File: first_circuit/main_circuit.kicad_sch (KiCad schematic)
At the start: 1 part

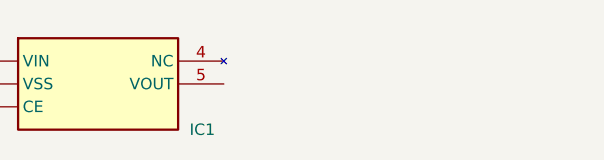
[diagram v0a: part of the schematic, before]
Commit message: need to create nets first
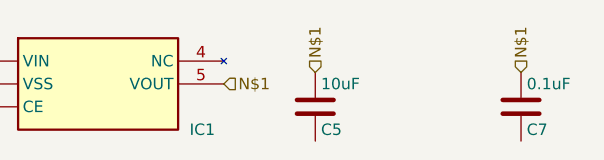
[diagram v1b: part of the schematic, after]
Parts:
- added C5: 10uF, Capacitor_SMD:C_0603, symbol Device:C
- added C7: 0.1uF, Capacitor_SMD:C_0603, symbol Device:C
- IC1: hierarchy_path /4697b12b-0876-4ea0-b477-ab5805670aa4 -> /acfeb8ae-789f-47ff-9243-69ba4f706be6; root_uuid 4697b12b-0876-4ea0-b477-ab5805670aa4 -> acfeb8ae-789f-47ff-9243-69ba4f706be6
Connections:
- net N$1: now reaches IC1.5 (VOUT)
- net N$1: now also C5.1, C7.1
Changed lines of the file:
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@@
 			)
 		)
-		(property "hierarchy_path" "/4697b12b-0876-4ea0-b477-ab5805670aa4"
+		(property "hierarchy_path" "/acfeb8ae-789f-47ff-9243-69ba4f706be6"
 			(at 43.18 33.0199 0)
 			(effects
@@
 			)
 		)
-		(property "root_uuid" "4697b12b-0876-4ea0-b477-ab5805670aa4"
+		(property "root_uuid" "acfeb8ae-789f-47ff-9243-69ba4f706be6"
 			(at 43.18 33.0199 0)
 			(effects
@@
 		(instances
 			(project ""
-				(path "/4697b12b-0876-4ea0-b477-ab5805670aa4"
+				(path "/acfeb8ae-789f-47ff-9243-69ba4f706be6"
 					(reference "IC1")
 					(unit 1)
@@
 		)
 	)
+	(symbol
+		(lib_id "Device:C")
+		(at 78.74 33.02 0)
+		(unit 1)
+		(exclude_from_sim no)
+		(in_bom yes)
+		(on_board yes)
+		(dnp no)
+		(fields_autoplaced no)
+		(property "Reference" "C5"
+			(at 79.375 35.56 0.0000)
+			(effects
+				(font
+					(size 1.27 1.27)
+				)
+				(justify left)
+			)
+		)
+		(property "Value" "10uF"
+			(at 79.375 30.48 0.0000)
+			(effects
+				(font
+					(size 1.27 1.27)
+				)
+				(justify left)
+			)
+		)
+		(property "Footprint" "Capacitor_SMD:C_0603"
+			(at 79.7052 29.21 0.0000)
+			(effects
+				(font
+					(size 1.27 1.27)
+				)
+				(hide yes)
+			)
+		)
+		(property "hierarchy_path" "/acfeb8ae-789f-47ff-9243-69ba4f706be6"
+			(at 81.28 38.0999 0)
+			(effects
+				(font
+					(size 1.27 1.27)
+				)
+				(hide yes)
+			)
+		)
+		(property "project_name" "main_circuit"
+			(at 81.28 38.0999 0)
+			(effects
+				(font
+					(size 1.27 1.27)
+				)
+				(hide yes)
+			)
+		)
+		(property "root_uuid" "acfeb8ae-789f-47ff-9243-69ba4f706be6"
+			(at 81.28 38.0999 0)
+			(effects
+				(font
+					(size 1.27 1.27)
+				)
+				(hide yes)
+			)
+		)
+		(pin "1"
+		)
+		(pin "2"
+		)
+		(instances
+			(project ""
+				(path "/acfeb8ae-789f-47ff-9243-69ba4f706be6"
+					(reference "C5")
+					(unit 1)
+				)
+			)
+		)
+	)
+	(symbol
+		(lib_id "Device:C")
+		(at 101.6 33.02 0)
+		(unit 1)
+		(exclude_from_sim no)
+		(in_bom yes)
+		(on_board yes)
+		(dnp no)
+		(fields_autoplaced no)
+		(property "Reference" "C7"
+			(at 102.235 35.56 0.0000)
+			(effects
+				(font
+					(size 1.27 1.27)
+				)
+				(justify left)
+			)
+		)
+		(property "Value" "0.1uF"
+			(at 102.235 30.48 0.0000)
+			(effects
+				(font
+					(size 1.27 1.27)
+				)
+				(justify left)
+			)
+		)
+		(property "Footprint" "Capacitor_SMD:C_0603"
+			(at 102.5652 29.21 0.0000)
+			(effects
+				(font
+					(size 1.27 1.27)
+				)
+				(hide yes)
+			)
+		)
+		(property "hierarchy_path" "/acfeb8ae-789f-47ff-9243-69ba4f706be6"
+			(at 104.14 38.0999 0)
+			(effects
+				(font
+					(size 1.27 1.27)
+				)
+				(hide yes)
+			)
+		)
+		(property "project_name" "main_circuit"
+			(at 104.14 38.0999 0)
+			(effects
+				(font
+					(size 1.27 1.27)
+				)
+				(hide yes)
+			)
+		)
+		(property "root_uuid" "acfeb8ae-789f-47ff-9243-69ba4f706be6"
+			(at 104.14 38.0999 0)
+			(effects
+				(font
+					(size 1.27 1.27)
+				)
+				(hide yes)
+			)
+		)
+		(pin "1"
+		)
+		(pin "2"
+		)
+		(instances
+			(project ""
+				(path "/acfeb8ae-789f-47ff-9243-69ba4f706be6"
+					(reference "C7")
+					(unit 1)
+				)
+			)
+		)
+	)
+	(hierarchical_label "N$1"
+		(shape input)
+		(at 68.58 30.48 0.0000)
+		(effects
+			(font
+				(size 1.27 1.27)
+			)
+			(justify left)
+		)
+	)
+	(hierarchical_label "N$1"
+		(shape input)
+		(at 78.74 29.21 90)
+		(effects
+			(font
+				(size 1.27 1.27)
+			)
+			(justify left)
+		)
+	)
+	(hierarchical_label "N$1"
+		(shape input)
+		(at 101.6 29.21 90)
+		(effects
+			(font
+				(size 1.27 1.27)
+			)
+			(justify left)
+		)
+	)

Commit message: nets
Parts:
- C5, C7: footprint Capacitor_SMD:C_0603 -> Capacitor_SMD:C_0201_0603Metric; hierarchy_path /acfeb8ae-789f-47ff-9243-69ba4f706be6 -> /e07d8eb1-7943-4b3e-9fa9-f711b15326a7; root_uuid acfeb8ae-789f-47ff-9243-69ba4f706be6 -> e07d8eb1-7943-4b3e-9fa9-f711b15326a7
- IC1: hierarchy_path /acfeb8ae-789f-47ff-9243-69ba4f706be6 -> /e07d8eb1-7943-4b3e-9fa9-f711b15326a7; root_uuid acfeb8ae-789f-47ff-9243-69ba4f706be6 -> e07d8eb1-7943-4b3e-9fa9-f711b15326a7
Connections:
- net N$1 renamed REGULATOR_VOUT
- net REGULATOR_VOUT: no longer C7.1
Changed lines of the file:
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@@
 			)
 		)
-		(property "hierarchy_path" "/acfeb8ae-789f-47ff-9243-69ba4f706be6"
+		(property "hierarchy_path" "/e07d8eb1-7943-4b3e-9fa9-f711b15326a7"
 			(at 43.18 33.0199 0)
 			(effects
@@
 			)
 		)
-		(property "root_uuid" "acfeb8ae-789f-47ff-9243-69ba4f706be6"
+		(property "root_uuid" "e07d8eb1-7943-4b3e-9fa9-f711b15326a7"
 			(at 43.18 33.0199 0)
 			(effects
@@
 		(instances
 			(project ""
-				(path "/acfeb8ae-789f-47ff-9243-69ba4f706be6"
+				(path "/e07d8eb1-7943-4b3e-9fa9-f711b15326a7"
 					(reference "IC1")
 					(unit 1)
@@
 			)
 		)
-		(property "Footprint" "Capacitor_SMD:C_0603"
+		(property "Footprint" "Capacitor_SMD:C_0201_0603Metric"
 			(at 79.7052 29.21 0.0000)
 			(effects
@@
 			)
 		)
-		(property "hierarchy_path" "/acfeb8ae-789f-47ff-9243-69ba4f706be6"
+		(property "hierarchy_path" "/e07d8eb1-7943-4b3e-9fa9-f711b15326a7"
 			(at 81.28 38.0999 0)
 			(effects
@@
 			)
 		)
-		(property "root_uuid" "acfeb8ae-789f-47ff-9243-69ba4f706be6"
+		(property "root_uuid" "e07d8eb1-7943-4b3e-9fa9-f711b15326a7"
 			(at 81.28 38.0999 0)
 			(effects
@@
 		(instances
 			(project ""
-				(path "/acfeb8ae-789f-47ff-9243-69ba4f706be6"
+				(path "/e07d8eb1-7943-4b3e-9fa9-f711b15326a7"
 					(reference "C5")
 					(unit 1)
@@
 			)
 		)
-		(property "Footprint" "Capacitor_SMD:C_0603"
+		(property "Footprint" "Capacitor_SMD:C_0201_0603Metric"
 			(at 102.5652 29.21 0.0000)
 			(effects
@@
 			)
 		)
-		(property "hierarchy_path" "/acfeb8ae-789f-47ff-9243-69ba4f706be6"
+		(property "hierarchy_path" "/e07d8eb1-7943-4b3e-9fa9-f711b15326a7"
 			(at 104.14 38.0999 0)
 			(effects
@@
 			)
 		)
-		(property "root_uuid" "acfeb8ae-789f-47ff-9243-69ba4f706be6"
+		(property "root_uuid" "e07d8eb1-7943-4b3e-9fa9-f711b15326a7"
 			(at 104.14 38.0999 0)
 			(effects
@@
 		(instances
 			(project ""
-				(path "/acfeb8ae-789f-47ff-9243-69ba4f706be6"
+				(path "/e07d8eb1-7943-4b3e-9fa9-f711b15326a7"
 					(reference "C7")
 					(unit 1)
@@
 		)
 	)
-	(hierarchical_label "N$1"
+	(hierarchical_label "REGULATOR_VOUT"
 		(shape input)
 		(at 68.58 30.48 0.0000)
@@
 		)
 	)
-	(hierarchical_label "N$1"
+	(hierarchical_label "REGULATOR_VOUT"
 		(shape input)
 		(at 78.74 29.21 90)
 		(effects
 			(font
-				(size 1.27 1.27)
-			)
-			(justify left)
-		)
-	)
-	(hierarchical_label "N$1"
-		(shape input)
-		(at 101.6 29.21 90)
-		(effects
-			(font

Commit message: start again
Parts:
- C5, C7, IC1: hierarchy_path /e07d8eb1-7943-4b3e-9fa9-f711b15326a7 -> /3fa41bdc-4b18-47ee-967e-f455cf70c87d; root_uuid e07d8eb1-7943-4b3e-9fa9-f711b15326a7 -> 3fa41bdc-4b18-47ee-967e-f455cf70c87d
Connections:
- net REGULATOR_VOUT: now also C7.1
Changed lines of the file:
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@@
 			)
 		)
-		(property "hierarchy_path" "/e07d8eb1-7943-4b3e-9fa9-f711b15326a7"
+		(property "hierarchy_path" "/3fa41bdc-4b18-47ee-967e-f455cf70c87d"
 			(at 43.18 33.0199 0)
 			(effects
@@
 			)
 		)
-		(property "root_uuid" "e07d8eb1-7943-4b3e-9fa9-f711b15326a7"
+		(property "root_uuid" "3fa41bdc-4b18-47ee-967e-f455cf70c87d"
 			(at 43.18 33.0199 0)
 			(effects
@@
 		(instances
 			(project ""
-				(path "/e07d8eb1-7943-4b3e-9fa9-f711b15326a7"
+				(path "/3fa41bdc-4b18-47ee-967e-f455cf70c87d"
 					(reference "IC1")
 					(unit 1)
@@
 			)
 		)
-		(property "hierarchy_path" "/e07d8eb1-7943-4b3e-9fa9-f711b15326a7"
+		(property "hierarchy_path" "/3fa41bdc-4b18-47ee-967e-f455cf70c87d"
 			(at 81.28 38.0999 0)
 			(effects
@@
 			)
 		)
-		(property "root_uuid" "e07d8eb1-7943-4b3e-9fa9-f711b15326a7"
+		(property "root_uuid" "3fa41bdc-4b18-47ee-967e-f455cf70c87d"
 			(at 81.28 38.0999 0)
 			(effects
@@
 		(instances
 			(project ""
-				(path "/e07d8eb1-7943-4b3e-9fa9-f711b15326a7"
+				(path "/3fa41bdc-4b18-47ee-967e-f455cf70c87d"
 					(reference "C5")
 					(unit 1)
@@
 			)
 		)
-		(property "hierarchy_path" "/e07d8eb1-7943-4b3e-9fa9-f711b15326a7"
+		(property "hierarchy_path" "/3fa41bdc-4b18-47ee-967e-f455cf70c87d"
 			(at 104.14 38.0999 0)
 			(effects
@@
 			)
 		)
-		(property "root_uuid" "e07d8eb1-7943-4b3e-9fa9-f711b15326a7"
+		(property "root_uuid" "3fa41bdc-4b18-47ee-967e-f455cf70c87d"
 			(at 104.14 38.0999 0)
 			(effects
@@
 		(instances
 			(project ""
-				(path "/e07d8eb1-7943-4b3e-9fa9-f711b15326a7"
+				(path "/3fa41bdc-4b18-47ee-967e-f455cf70c87d"
 					(reference "C7")
 					(unit 1)
@@
 		(effects
 			(font
+				(size 1.27 1.27)
+			)
+			(justify left)
+		)
+	)
+	(hierarchical_label "REGULATOR_VOUT"
+		(shape input)
+		(at 101.6 29.21 90)
+		(effects
+			(font

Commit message: start again
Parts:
- removed C5: 10uF, Capacitor_SMD:C_0201_0603Metric, symbol Device:C
- removed C7: 0.1uF, Capacitor_SMD:C_0201_0603Metric, symbol Device:C
- removed IC1: (no value), SamacSys_Parts:SOT95P280X130-5N, symbol SamacSys_Parts:XC6220B331MR-G
- added J1: (no value), SamacSys_Parts:USB4135GFA, symbol SamacSys_Parts:USB4135-GF-A
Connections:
- new net GND: J1.B12, J1.MP1, J1.MP2, J1.MP3, J1.MP4

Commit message: rc_delay
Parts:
- removed J1: (no value), SamacSys_Parts:USB4135GFA, symbol SamacSys_Parts:USB4135-GF-A
- added C12: 1uF, Capacitor_SMD:C_0603_1608Metric, symbol Device:C
- added R3: 10k, Resistor_SMD:R_0603_1608Metric, symbol Device:R
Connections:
- net GND: now also C12.2
- new net +3.3V: R3.1
- new net EN: C12.1, R3.2
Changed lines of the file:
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@@
 	)
 	(symbol
-		(lib_id "SamacSys_Parts:USB4135-GF-A")
-		(at 40.64 30.48 0)
-		(unit 1)
-		(exclude_from_sim no)
-		(in_bom yes)
-		(on_board yes)
-		(dnp no)
-		(fields_autoplaced no)
-		(property "Reference" "J1"
-			(at 62.23 38.1 0.0000)
-			(effects
-				(font
-					(size 1.27 1.27)
-				)
-				(justify left)
-			)
-		)
-		(property "Footprint" "SamacSys_Parts:USB4135GFA"
-			(at 62.23 -64.44 0.0000)
-			(effects
-				(font
-					(size 1.27 1.27)
-				)
-				(hide yes)
-			)
-		)
-		(property "hierarchy_path" "/74824406-cd07-43be-b55f-f7d501532b0e"
-			(at 43.18 35.5599 0)
+		(lib_id "Device:R")
+		(at 30.48 35.56 0)
+		(unit 1)
+		(exclude_from_sim no)
+		(in_bom yes)
+		(on_board yes)
+		(dnp no)
+		(fields_autoplaced no)
+		(property "Reference" "R3"
+			(at 32.512 35.56 90)
+			(effects
+				(font
+					(size 1.27 1.27)
+				)
+				(justify left)
+			)
+		)
+		(property "Value" "10k"
+			(at 30.48 35.56 90)
+			(effects
+				(font
+					(size 1.27 1.27)
+				)
+				(justify left)
+			)
+		)
+		(property "Footprint" "Resistor_SMD:R_0603_1608Metric"
+			(at 28.702 35.56 90)
+			(effects
+				(font
+					(size 1.27 1.27)
+				)
+				(hide yes)
+			)
+		)
+		(property "hierarchy_path" "/18790e42-201e-4808-bfa1-f33409c8c696"
+			(at 33.02 40.6399 0)
 			(effects
 				(font
@@
 		)
 		(property "project_name" "main_circuit"
-			(at 43.18 35.5599 0)
-			(effects
-				(font
-					(size 1.27 1.27)
-				)
-				(hide yes)
-			)
-		)
-		(property "root_uuid" "74824406-cd07-43be-b55f-f7d501532b0e"
-			(at 43.18 35.5599 0)
-			(effects
-				(font
-					(size 1.27 1.27)
-				)
-				(hide yes)
-			)
-		)
-		(pin "A5"
-		)
-		(pin "A9"
-		)
-		(pin "A12"
-		)
-		(pin "B5"
-		)
-		(pin "B9"
-		)
-		(pin "B12"
-		)
-		(pin "MP1"
-		)
-		(pin "MP2"
-		)
-		(pin "MP3"
-		)
-		(pin "MP4"
-		)
-		(instances
-			(project ""
-				(path "/74824406-cd07-43be-b55f-f7d501532b0e"
-					(reference "J1")
-					(unit 1)
-				)
-			)
-		)
-	)
-	(symbol
-		(lib_id "power:GND")
-		(at 66.04 30.48 90)
+			(at 33.02 40.6399 0)
+			(effects
+				(font
+					(size 1.27 1.27)
+				)
+				(hide yes)
+			)
+		)
+		(property "root_uuid" "18790e42-201e-4808-bfa1-f33409c8c696"
+			(at 33.02 40.6399 0)
+			(effects
+				(font
+					(size 1.27 1.27)
+				)
+				(hide yes)
+			)
+		)
+		(pin "1"
+		)
+		(pin "2"
+		)
+		(instances
+			(project ""
+				(path "/18790e42-201e-4808-bfa1-f33409c8c696"
+					(reference "R3")
+					(unit 1)
+				)
+			)
+		)
+	)
+	(symbol
+		(lib_id "Device:C")
+		(at 55.88 33.02 0)
+		(unit 1)
+		(exclude_from_sim no)
+		(in_bom yes)
+		(on_board yes)
+		(dnp no)
+		(fields_autoplaced no)
+		(property "Reference" "C12"
+			(at 56.515 35.56 0.0000)
+			(effects
+				(font
+					(size 1.27 1.27)
+				)
+				(justify left)
+			)
+		)
+		(property "Value" "1uF"
+			(at 56.515 30.48 0.0000)
+			(effects
+				(font
+					(size 1.27 1.27)
+				)
+				(justify left)
+			)
+		)
+		(property "Footprint" "Capacitor_SMD:C_0603_1608Metric"
+			(at 56.8452 29.21 0.0000)
+			(effects
+				(font
+					(size 1.27 1.27)
+				)
+				(hide yes)
+			)
+		)
+		(property "hierarchy_path" "/18790e42-201e-4808-bfa1-f33409c8c696"
+			(at 58.42 38.0999 0)
+			(effects
+				(font
+					(size 1.27 1.27)
+				)
+				(hide yes)
+			)
+		)
+		(property "project_name" "main_circuit"
+			(at 58.42 38.0999 0)
+			(effects
+				(font
+					(size 1.27 1.27)
+				)
+				(hide yes)
+			)
+		)
+		(property "root_uuid" "18790e42-201e-4808-bfa1-f33409c8c696"
+			(at 58.42 38.0999 0)
+			(effects
+				(font
+					(size 1.27 1.27)
+				)
+				(hide yes)
+			)
+		)
+		(pin "1"
+		)
+		(pin "2"
+		)
+		(instances
+			(project ""
+				(path "/18790e42-201e-4808-bfa1-f33409c8c696"
+					(reference "C12")
+					(unit 1)
+				)
+			)
+		)
+	)
+	(symbol
+		(lib_id "power:+3V3")
+		(at 30.48 31.75 0)
 		(unit 1)
 		(exclude_from_sim no)
@@
 		(fields_autoplaced no)
 		(property "Reference" "#PWR001"
-			(at 72.39 30.48 90)
-			(effects
-				(font
-					(size 1.27 1.27)
-				)
-				(justify left)
-				(hide yes)
-			)
-		)
-		(property "Value" "GND"
-			(at 71.11999999999999 30.48 0)
+			(at 30.48 27.94 0.0000)
+			(effects
+				(font
+					(size 1.27 1.27)
+				)
+				(justify left)
+				(hide yes)
+			)
+		)
+		(property "Value" "+3.3V"
+			(at 30.48 26.67 0)
 			(effects
 				(font
@@
 		)
 		(property "Footprint" ""
-			(at 66.04 30.48 0.0000)
+			(at 30.48 31.75 0.0000)
 			(effects
 				(font
@@
 	(symbol
 		(lib_id "power:GND")
-		(at 66.04 33.02 90)
+		(at 55.88 36.83 0)
 		(unit 1)
 		(exclude_from_sim no)
@@
 		(fields_autoplaced no)
 		(property "Reference" "#PWR002"
-			(at 72.39 33.02 90)
+			(at 55.88 30.48 0.0000)
 			(effects
 				(font
@@
 		)
 		(property "Value" "GND"
-			(at 71.11999999999999 33.02 0)
+			(at 55.88 41.910000000000004 0)
 			(effects
 				(font
@@
 		)
 		(property "Footprint" ""
-			(at 66.04 33.02 0.0000)
+			(at 55.88 36.83 0.0000)
 			(effects
 				(font
@@
 		)
 	)
-	(symbol
-		(lib_id "power:GND")
-		(at 66.04 35.56 90)
-		(unit 1)
-		(exclude_from_sim no)
-		(in_bom yes)
-		(on_board yes)
-		(dnp no)
-		(fields_autoplaced no)
-		(property "Reference" "#PWR003"
-			(at 72.39 35.56 90)
-			(effects
-				(font
-					(size 1.27 1.27)
-				)
-				(justify left)
-				(hide yes)
-			)
-		)
-		(property "Value" "GND"
-			(at 71.11999999999999 35.56 0)
-			(effects
-				(font
-					(size 1.27 1.27)
-				)
-			)
-		)
-		(property "Footprint" ""
-			(at 66.04 35.56 0.0000)
-			(effects
-				(font
-					(size 1.27 1.27)
-				)
-				(hide yes)
-			)
-		)
-		(pin "1"
-		)
-		(instances
-			(project ""
-				(path "/"
-					(reference "#PWR003")
-					(unit 1)
-				)
-			)
-		)
-	)
-	(symbol
-		(lib_id "power:GND")
-		(at 66.04 38.1 90)
-		(unit 1)
-		(exclude_from_sim no)
-		(in_bom yes)
-		(on_board yes)
-		(dnp no)
-		(fields_autoplaced no)
-		(property "Reference" "#PWR004"
-			(at 72.39 38.1 90)
-			(effects
-				(font
-					(size 1.27 1.27)
-				)
-				(justify left)
-				(hide yes)
-			)
-		)
-		(property "Value" "GND"
-			(at 71.11999999999999 38.1 0)
-			(effects
-				(font
-					(size 1.27 1.27)
-				)
-			)
-		)
-		(property "Footprint" ""
-			(at 66.04 38.1 0.0000)
-			(effects
-				(font
-					(size 1.27 1.27)
-				)
-				(hide yes)
-			)
-		)
-		(pin "1"
-		)
-		(instances
-			(project ""
-				(path "/"
-					(reference "#PWR004")
-					(unit 1)
-				)
-			)
-		)
-	)
-	(symbol
-		(lib_id "power:GND")
-		(at 66.04 40.64 90)
-		(unit 1)
-		(exclude_from_sim no)
-		(in_bom yes)
-		(on_board yes)
-		(dnp no)
-		(fields_autoplaced no)
-		(property "Reference" "#PWR005"
-			(at 72.39 40.64 90)
-			(effects
-				(font
-					(size 1.27 1.27)
-				)
-				(justify left)
-				(hide yes)
-			)
-		)
-		(property "Value" "GND"
-			(at 71.11999999999999 40.64 0)
-			(effects
-				(font
-					(size 1.27 1.27)
-				)
-			)
-		)
-		(property "Footprint" ""
-			(at 66.04 40.64 0.0000)
-			(effects
-				(font
-					(size 1.27 1.27)
-				)
-				(hide yes)
-			)
-		)
-		(pin "1"
-		)
-		(instances
-			(project ""
-				(path "/"
-					(reference "#PWR005")
-					(unit 1)
-				)
-			)
-		)
-	)
+	(hierarchical_label "EN"
+		(shape input)
+		(at 30.48 39.37 270)
+		(effects
+			(font
+				(size 1.27 1.27)
+			)
+			(justify right)
+		)
+	)
+	(hierarchical_label "EN"
+		(shape input)
+		(at 55.88 29.21 90)
+		(effects
+			(font
+				(size 1.27 1.27)
+			)
+			(justify left)
+		)
+	)

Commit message: uart
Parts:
- removed C12: 1uF, Capacitor_SMD:C_0603_1608Metric, symbol Device:C
- removed R3: 10k, Resistor_SMD:R_0603_1608Metric, symbol Device:R
- added J3: UART_Header, Connector_PinHeader_2.54mm:PinHeader_1x03_P2.54mm_Vertical, symbol Connector_Generic:Conn_01x03
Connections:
- net GND: now also J3.1 (Pin_1)
- new net RXD: J3.3 (Pin_3)
- new net TXD: J3.2 (Pin_2)
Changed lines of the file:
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@@
 	)
 	(symbol
-		(lib_id "Device:R")
-		(at 30.48 35.56 0)
+		(lib_id "Connector_Generic:Conn_01x03")
+		(at 30.48 27.94 0)
 		(unit 1)
 		(exclude_from_sim no)
@@
 		(dnp no)
 		(fields_autoplaced no)
-		(property "Reference" "R3"
-			(at 32.512 35.56 90)
+		(property "Reference" "J3"
+			(at 30.48 33.02 0.0000)
 			(effects
 				(font
@@
 			)
 		)
-		(property "Value" "10k"
-			(at 30.48 35.56 90)
+		(property "Value" "UART_Header"
+			(at 30.48 22.86 0.0000)
 			(effects
 				(font
@@
 			)
 		)
-		(property "Footprint" "Resistor_SMD:R_0603_1608Metric"
-			(at 28.702 35.56 90)
+		(property "Footprint" "Connector_PinHeader_2.54mm:PinHeader_1x03_P2.54mm_Vertical"
+			(at 30.48 27.94 0.0000)
 			(effects
 				(font
@@
 			)
 		)
-		(property "hierarchy_path" "/18790e42-201e-4808-bfa1-f33409c8c696"
-			(at 33.02 40.6399 0)
+		(property "hierarchy_path" "/d6d32006-2e24-439e-8123-b988d5d2a167"
+			(at 33.02 33.0199 0)
 			(effects
 				(font
@@
 		)
 		(property "project_name" "main_circuit"
-			(at 33.02 40.6399 0)
+			(at 33.02 33.0199 0)
 			(effects
 				(font
@@
 			)
 		)
-		(property "root_uuid" "18790e42-201e-4808-bfa1-f33409c8c696"
-			(at 33.02 40.6399 0)
+		(property "root_uuid" "d6d32006-2e24-439e-8123-b988d5d2a167"
+			(at 33.02 33.0199 0)
 			(effects
 				(font
@@
 		(pin "2"
 		)
+		(pin "3"
+		)
 		(instances
 			(project ""
-				(path "/18790e42-201e-4808-bfa1-f33409c8c696"
-					(reference "R3")
+				(path "/d6d32006-2e24-439e-8123-b988d5d2a167"
+					(reference "J3")
 					(unit 1)
 				)
@@
 	)
 	(symbol
-		(lib_id "Device:C")
-		(at 55.88 33.02 0)
-		(unit 1)
-		(exclude_from_sim no)
-		(in_bom yes)
-		(on_board yes)
-		(dnp no)
-		(fields_autoplaced no)
-		(property "Reference" "C12"
-			(at 56.515 35.56 0.0000)
-			(effects
-				(font
-					(size 1.27 1.27)
-				)
-				(justify left)
-			)
-		)
-		(property "Value" "1uF"
-			(at 56.515 30.48 0.0000)
-			(effects
-				(font
-					(size 1.27 1.27)
-				)
-				(justify left)
-			)
-		)
-		(property "Footprint" "Capacitor_SMD:C_0603_1608Metric"
-			(at 56.8452 29.21 0.0000)
-			(effects
-				(font
-					(size 1.27 1.27)
-				)
-				(hide yes)
-			)
-		)
-		(property "hierarchy_path" "/18790e42-201e-4808-bfa1-f33409c8c696"
-			(at 58.42 38.0999 0)
-			(effects
-				(font
-					(size 1.27 1.27)
-				)
-				(hide yes)
-			)
-		)
-		(property "project_name" "main_circuit"
-			(at 58.42 38.0999 0)
-			(effects
-				(font
-					(size 1.27 1.27)
-				)
-				(hide yes)
-			)
-		)
-		(property "root_uuid" "18790e42-201e-4808-bfa1-f33409c8c696"
-			(at 58.42 38.0999 0)
-			(effects
-				(font
-					(size 1.27 1.27)
-				)
-				(hide yes)
-			)
-		)
-		(pin "1"
-		)
-		(pin "2"
-		)
-		(instances
-			(project ""
-				(path "/18790e42-201e-4808-bfa1-f33409c8c696"
-					(reference "C12")
-					(unit 1)
-				)
-			)
-		)
-	)
-	(symbol
-		(lib_id "power:+3V3")
-		(at 30.48 31.75 0)
+		(lib_id "power:GND")
+		(at 25.4 25.4 270)
 		(unit 1)
 		(exclude_from_sim no)
@@
 		(fields_autoplaced no)
 		(property "Reference" "#PWR001"
-			(at 30.48 27.94 0.0000)
+			(at 19.05 25.4 270)
 			(effects
 				(font
@@
 			)
 		)
-		(property "Value" "+3.3V"
-			(at 30.48 26.67 0)
+		(property "Value" "GND"
+			(at 20.32 25.400000000000002 0)
 			(effects
 				(font
@@
 		)
 		(property "Footprint" ""
-			(at 30.48 31.75 0.0000)
+			(at 25.4 25.4 0.0000)
 			(effects
 				(font
@@
 		)
 	)
-	(symbol
-		(lib_id "power:GND")
-		(at 55.88 36.83 0)
-		(unit 1)
-		(exclude_from_sim no)
-		(in_bom yes)
-		(on_board yes)
-		(dnp no)
-		(fields_autoplaced no)
-		(property "Reference" "#PWR002"
-			(at 55.88 30.48 0.0000)
-			(effects
-				(font
-					(size 1.27 1.27)
-				)
-				(justify left)
-				(hide yes)
-			)
-		)
-		(property "Value" "GND"
-			(at 55.88 41.910000000000004 0)
-			(effects
-				(font
-					(size 1.27 1.27)
-				)
-			)
-		)
-		(property "Footprint" ""
-			(at 55.88 36.83 0.0000)
-			(effects
-				(font
-					(size 1.27 1.27)
-				)
-				(hide yes)
-			)
-		)
-		(pin "1"
-		)
-		(instances
-			(project ""
-				(path "/"
-					(reference "#PWR002")
-					(unit 1)
-				)
-			)
-		)
-	)
-	(hierarchical_label "EN"
+	(hierarchical_label "TXD"
 		(shape input)
-		(at 30.48 39.37 270)
+		(at 25.4 27.94 180)
 		(effects
 			(font
@@
 		)
 	)
-	(hierarchical_label "EN"
+	(hierarchical_label "RXD"
 		(shape input)
-		(at 55.88 29.21 90)
+		(at 25.4 30.48 180)
 		(effects
 			(font
 				(size 1.27 1.27)
 			)
-			(justify left)
+			(justify right)
 		)
 	)
